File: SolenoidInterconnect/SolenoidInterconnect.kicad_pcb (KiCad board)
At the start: 2 copper layers, 71.4 x 44 mm, 12 parts, among them J1 Screw_Terminal_01x02, J10 Screw_Terminal_01x02, J2 Screw_Terminal_01x02, J3 Screw_Terminal_01x02, J4 Screw_Terminal_01x02, J5 16PIN_OUT, J6 Screw_Terminal_01x02, J7 16PIN_IN, J8 Screw_Terminal_01x02, J9 Screw_Terminal_01x02

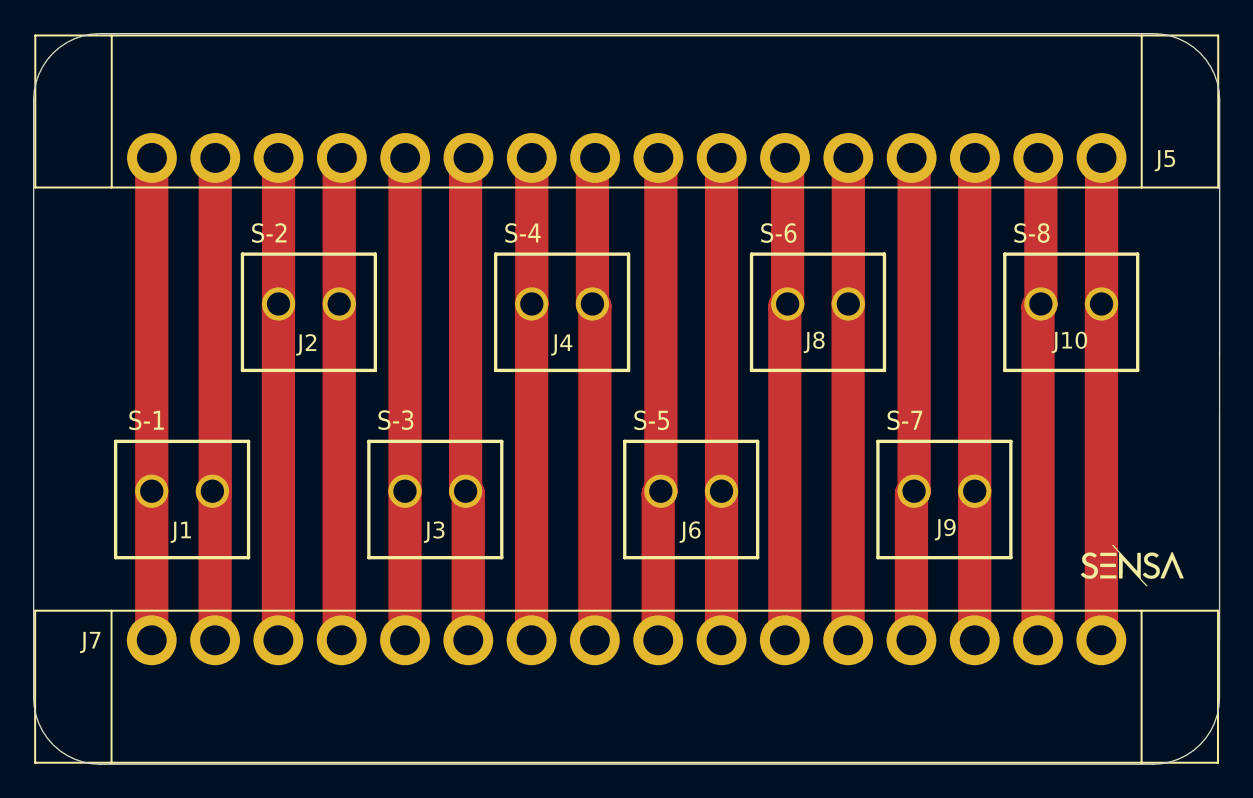
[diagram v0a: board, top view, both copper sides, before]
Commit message: Added mounting points
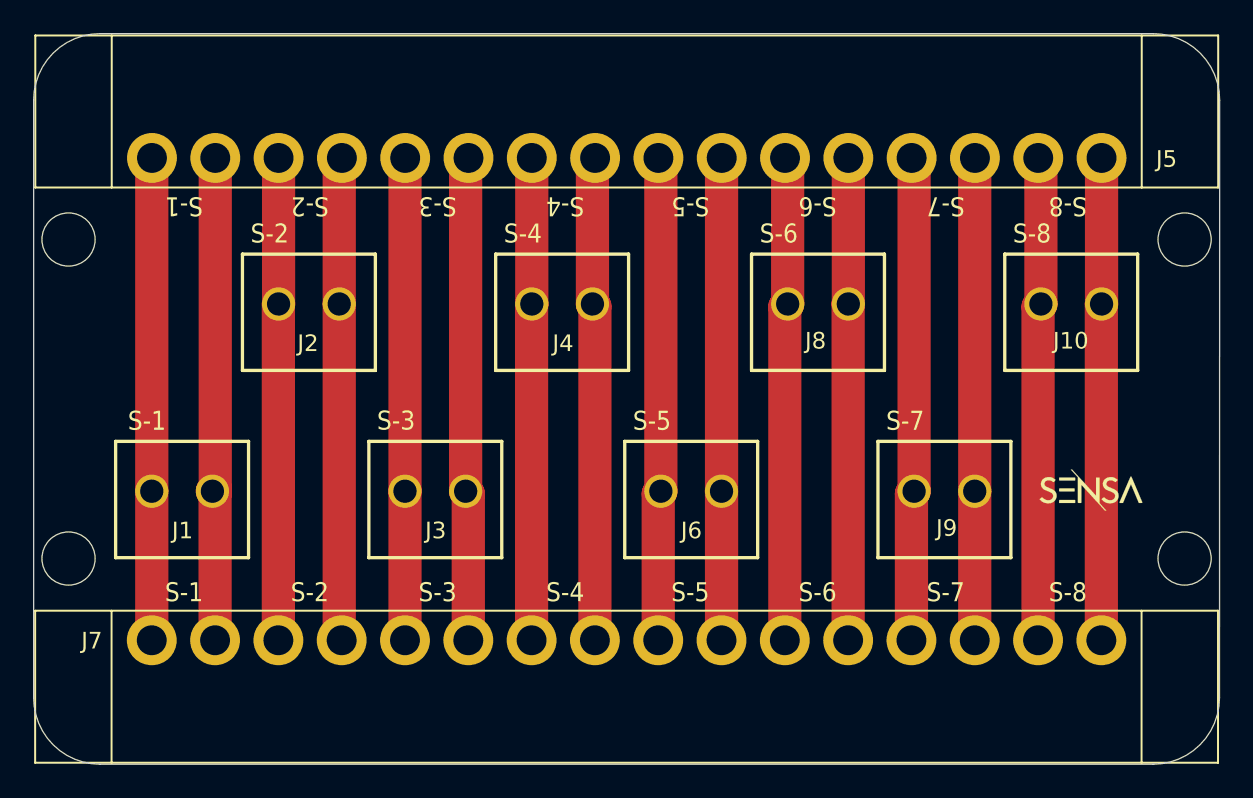
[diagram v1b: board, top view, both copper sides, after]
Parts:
- added REF**: MountingHole_3.2mm_M3_DIN965, MountingHole:MountingHole_3.2mm_M3_DIN965, F.Cu at (97.8, 106.0)
- added REF**: MountingHole_3.2mm_M3_DIN965, MountingHole:MountingHole_3.2mm_M3_DIN965, F.Cu at (97.8, 86.8)
- added REF**: MountingHole_3.2mm_M3_DIN965, MountingHole:MountingHole_3.2mm_M3_DIN965, F.Cu at (164.9, 86.8)
- added REF**: MountingHole_3.2mm_M3_DIN965, MountingHole:MountingHole_3.2mm_M3_DIN965, F.Cu at (164.9, 106.0)
- moved G*** 5.17 mm to (159.2, 101.9)
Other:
- board text added: "S-1"
- board text added: "S-2"
- board text added: "S-3"
- board text added: "S-4"
- board text added: "S-5"
- board text added: "S-6"
- board text added: "S-7"
- board text added: "S-8"
